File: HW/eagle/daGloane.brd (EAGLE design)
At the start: 100 x 80 mm, 90 parts, among them IC1 MCP1252-33X50, U1 STM32F10XTXU6, X2 SPARKFUN-CONNECTORS_USB-MICROB

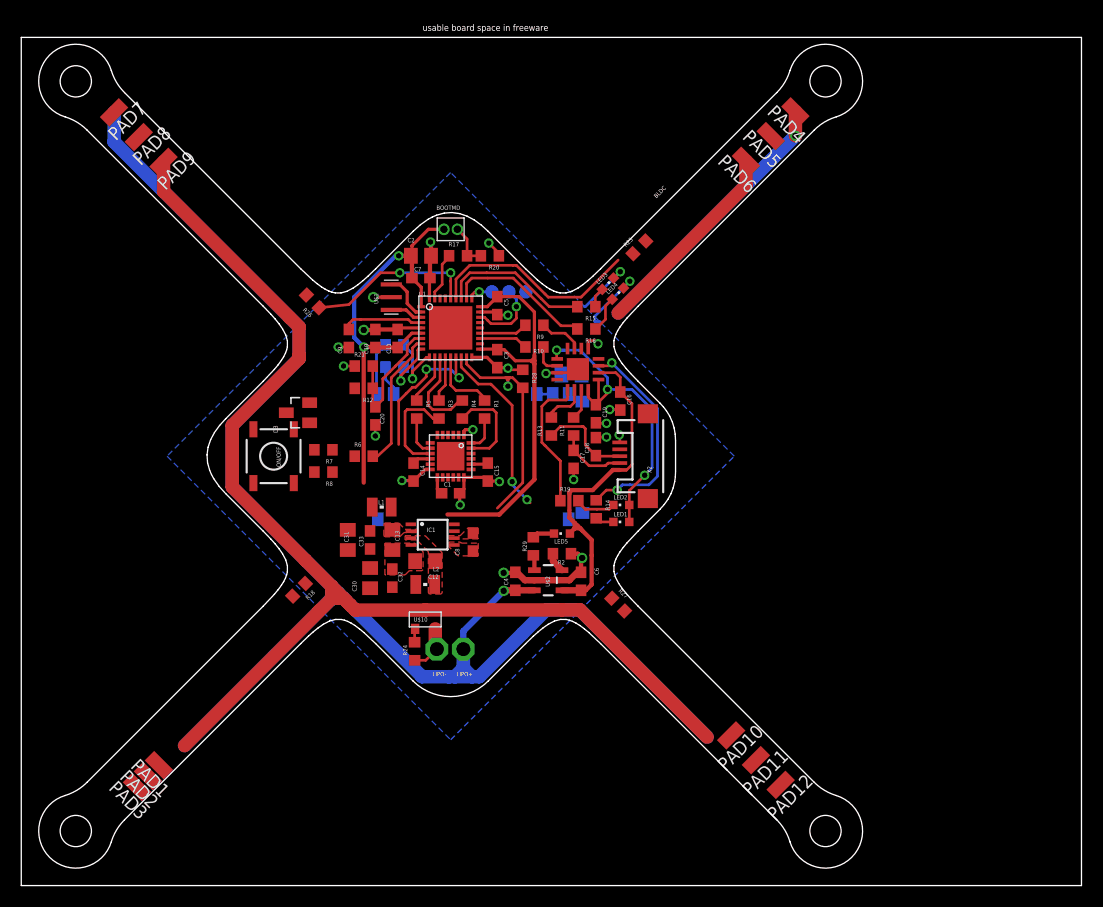
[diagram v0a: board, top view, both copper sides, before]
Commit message: DC/DC layout done
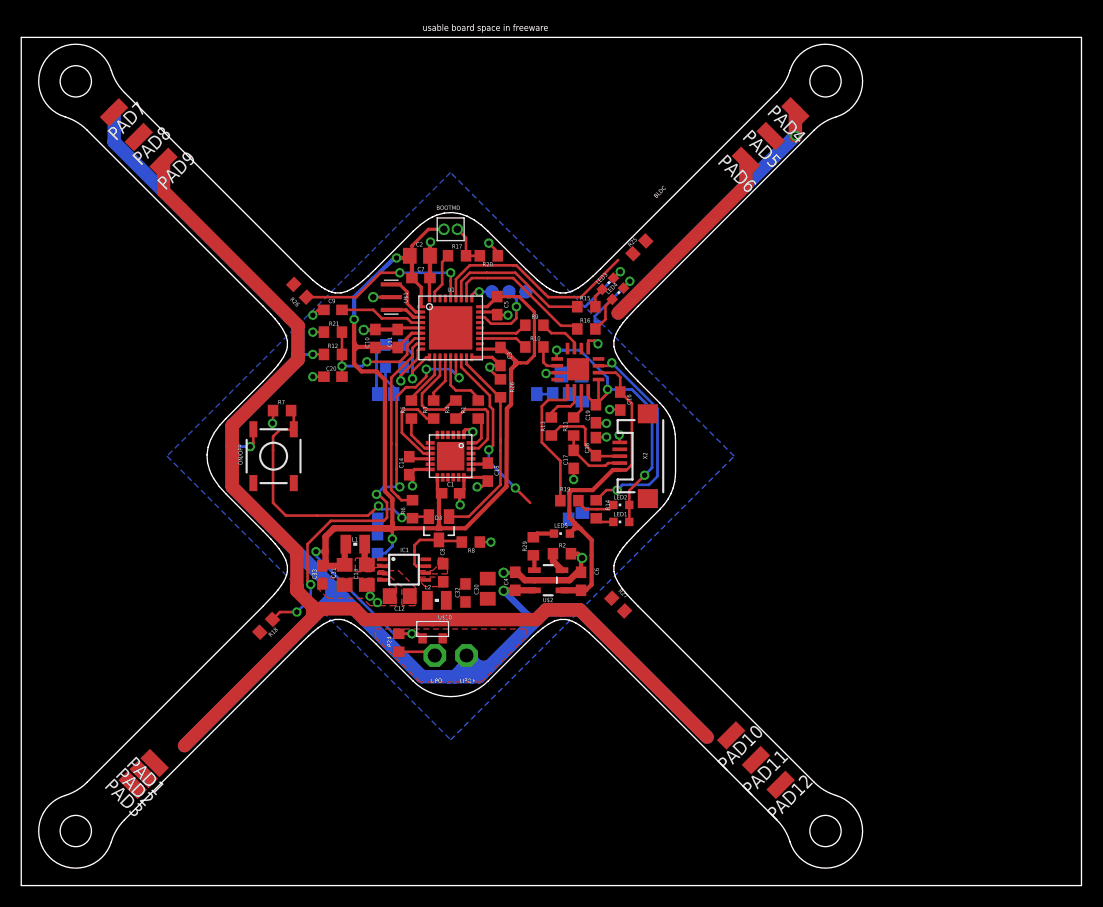
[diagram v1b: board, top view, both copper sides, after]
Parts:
- added R30: 1k, rcl:R0603
- moved D3 17.2 mm to (39.4, 33.7), turned to 180 degrees
- moved R8 15.4 mm to (42.4, 32.4)
- moved C30 11.1 mm to (44.0, 28.0)
- moved C32 7.04 mm to (41.9, 27.6)
- moved R6 6.79 mm to (36.9, 35.5), turned to 90 degrees
- moved C33 5.58 mm to (28.4, 29.3)
- moved C20 5.45 mm to (29.4, 48.0), turned to 180 degrees
- moved R7 5.38 mm to (24.6, 44.8), turned to 0 degrees
- moved R18 4.60 mm to (23.1, 24.5)
- moved R12 4.32 mm to (29.4, 50.1)
- moved R21 4.32 mm to (29.4, 52.2)
- moved L1 4.30 mm to (31.5, 32.2)
- moved IC1 4.26 mm to (36.1, 29.8)
- moved C12 4.08 mm to (35.7, 27.3)
- moved C13 4.08 mm to (32.6, 29.3)
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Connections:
- new net N$26: R30.1, U$5.P$34
- net VCC: now also R30.2; no longer U$5.P$34
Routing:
- net VCC: track 83.0 -> 133.1 mm, vias 2 -> 5
- net MOT1: track 13.8 -> 41.8 mm, vias 2 -> 6
- net N$23: track 0.00 -> 26.4 mm, vias 0 -> 2
- net LIPO: track 168.5 -> 176.6 mm, vias 2 -> 4
- net PWR_ON: track 0.00 -> 7.52 mm
- net PWR_OFF: track 13.0 -> 17.6 mm
- net GND: track 74.7 -> 76.8 mm, vias 24 -> 28
- net N$46: track 0.00 -> 2.04 mm
- net N$26: track 0.00 -> 1.51 mm
- net PWR_ON_µC: track 20.8 -> 19.5 mm, vias 1 -> 0
- net N$13: track 9.02 -> 7.96 mm
- net MOT4: track 16.1 -> 17.0 mm
- net VOLTAGE: track 12.6 -> 13.2 mm, vias 0 -> 2
- net N$18: track 9.52 -> 8.89 mm
- net SPI1_MOSI: track 6.57 -> 5.97 mm

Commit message: layout of center piece is done!
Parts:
- moved R14 15.1 mm to (52.0, 50.4), turned to 0 degrees
- moved LED1 12.7 mm to (54.9, 46.9), turned to 270 degrees
- moved C6 7.72 mm to (46.6, 33.3), turned to 0 degrees
- moved R2 7.00 mm to (44.0, 31.5), turned to 90 degrees
- moved C17 3.89 mm to (49.4, 37.4)
- moved R11 3.89 mm to (49.4, 40.5)
- moved R13 3.89 mm to (47.3, 40.5)
- moved U$2 3.58 mm to (46.5, 30.4), turned to 0 degrees
- moved C19 3.55 mm to (51.5, 42.2)
- moved C18 3.48 mm to (51.5, 39.2)
- moved R27 3.45 mm to (58.0, 23.5)
- moved U$4 3.32 mm to (50.1, 46.4)
- moved C16 2.66 mm to (54.0, 44.8)
- moved R29 2.60 mm to (49.3, 29.6)
- moved LED2 2.48 mm to (54.9, 34.1)
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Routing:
- net LIPO: track 176.6 -> 219.2 mm, vias 4 -> 6
- net MOT_GND: track 134.7 -> 157.8 mm
- net N$22: track 0.00 -> 20.4 mm
- net MOT2: track 16.7 -> 34.3 mm, vias 2 -> 6
- net N$11: track 20.6 -> 5.24 mm, vias 2 -> 0
- net VCC: track 133.1 -> 144.4 mm, vias 5 -> 6
- net N$43: track 1.42 -> 7.11 mm, vias 0 -> 2
- net D+: track 8.87 -> 12.2 mm
- net D-: track 6.52 -> 9.82 mm
- net N$14: track 1.76 -> 4.64 mm
- net N$21: track 2.88 -> 5.70 mm
- net N$1: track 3.98 -> 1.57 mm
- net N$12: track 13.2 -> 15.1 mm
- net GND: track 76.8 -> 78.3 mm, vias 28 -> 29
- net LED1: track 14.2 -> 12.9 mm
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- added copper zone on layer 1, net LIPO
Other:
- board text removed: "BLDC"

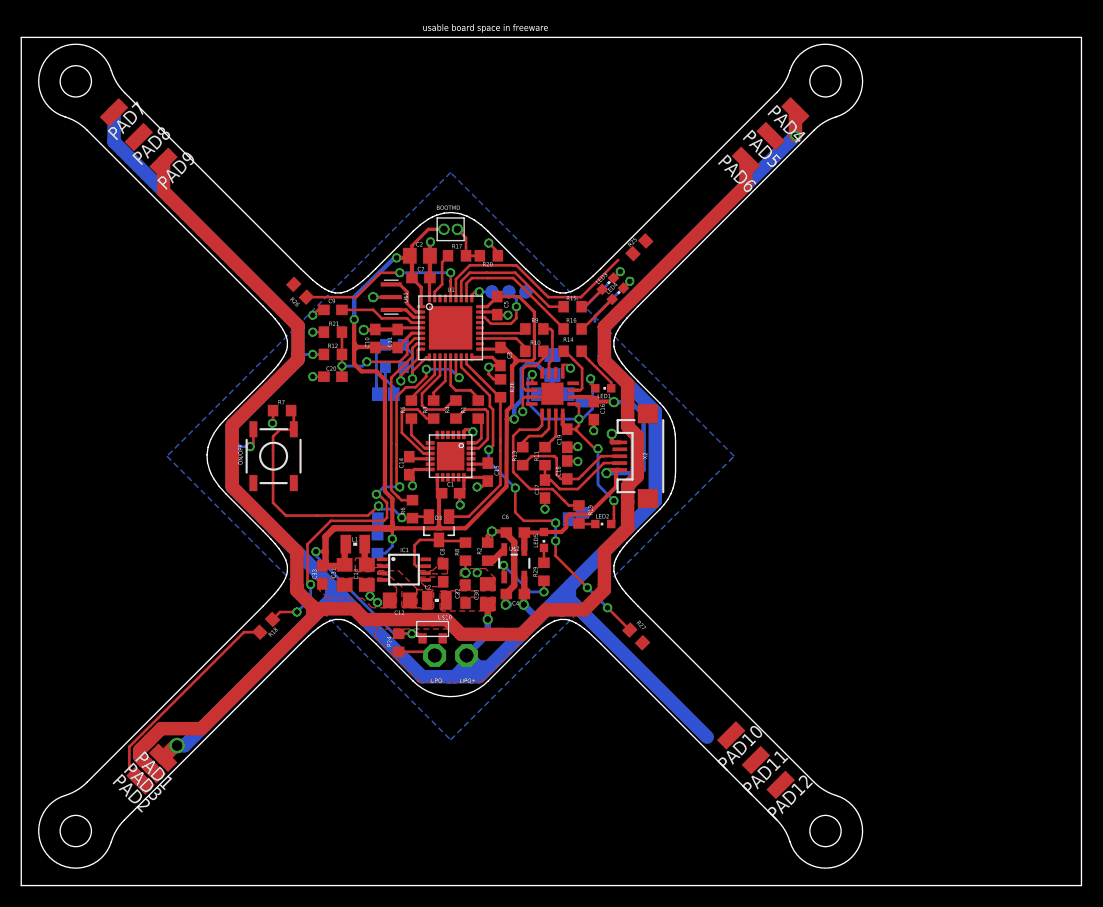
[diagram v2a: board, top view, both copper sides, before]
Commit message: testpads replaced with HK03 bldc controller symbol & package
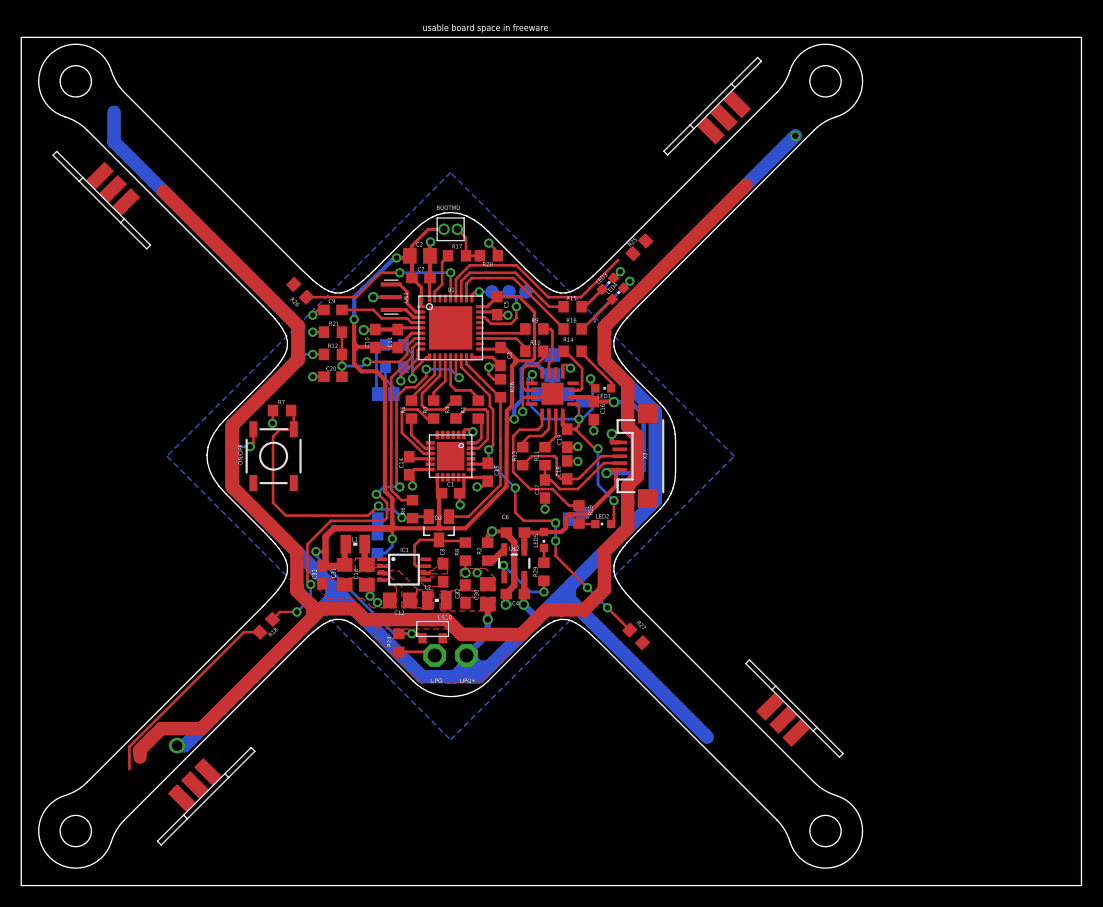
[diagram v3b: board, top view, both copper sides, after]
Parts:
- removed PAD1, PAD10, PAD11, PAD12, PAD2, PAD3, PAD4, PAD5, PAD6, PAD7, PAD8, PAD9: (no value), daGloane:SMD1,27-2,54
- added U$6, U$7, U$8, U$9: 3A_BLDC_CONTROLLER, daGloane:3A_BLDC_CONTROLLER
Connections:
- net LIPO: now also U$6.2, U$7.2, U$8.2, U$9.2; no longer PAD1.1, PAD10.1, PAD4.1, PAD7.1
- net MOT_GND: now also U$6.1, U$7.1, U$8.1, U$9.1; no longer PAD12.1, PAD3.1, PAD6.1, PAD9.1
- net N$22: now also U$6.3; no longer PAD2.1
- net N$39: now also U$7.3; no longer PAD11.1
- net N$40: now also U$8.3; no longer PAD5.1
- net N$41: now also U$9.3; no longer PAD8.1
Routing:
- net MOT_GND: track 157.8 -> 151.2 mm
- net LIPO: track 219.2 -> 215.2 mm
- net N$22: track 20.4 -> 18.9 mm
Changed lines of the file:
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@@
 <attribute name="VALUE" x="55.934540625" y="22.691778125" size="0.4064" layer="27" rot="R315"/>
 </element>
-<element name="PAD1" library="daGloane" package="SMD1,27-2,54" value="" x="13.38700625" y="12.055634375" rot="R45"/>
-<element name="PAD2" library="daGloane" package="SMD1,27-2,54" value="" x="11.25355625" y="9.92218125" rot="R45"/>
-<element name="PAD3" library="daGloane" package="SMD1,27-2,54" value="" x="12.320103125" y="10.988728125" rot="R45"/>
-<element name="PAD4" library="daGloane" package="SMD1,27-2,54" value="" x="73.018378125" y="73.028425" rot="R45"/>
-<element name="PAD5" library="daGloane" package="SMD1,27-2,54" value="" x="70.684925" y="70.694971875" rot="R45"/>
-<element name="PAD6" library="daGloane" package="SMD1,27-2,54" value="" x="68.351471875" y="68.361521875" rot="R45"/>
-<element name="PAD7" library="daGloane" package="SMD1,27-2,54" value="" x="8.752334375" y="72.93345" rot="R135"/>
-<element name="PAD8" library="daGloane" package="SMD1,27-2,54" value="" x="11.0857875" y="70.6" rot="R135"/>
-<element name="PAD9" library="daGloane" package="SMD1,27-2,54" value="" x="13.419240625" y="68.26655" rot="R135"/>
-<element name="PAD10" library="daGloane" package="SMD1,27-2,54" value="" x="66.95944375" y="14.164821875" rot="R135"/>
-<element name="PAD11" library="daGloane" package="SMD1,27-2,54" value="" x="69.29289375" y="11.83136875" rot="R135"/>
-<element name="PAD12" library="daGloane" package="SMD1,27-2,54" value="" x="71.626346875" y="9.497915625" rot="R135"/>
 <element name="R28" library="rcl" package="R0603" value="10k" x="45.2" y="46.9" smashed="yes" rot="R270">
 <attribute name="NAME" x="46.089" y="47.489" size="0.4064" layer="25" rot="R270"/>
@@
 <attribute name="VALUE" x="35.632" y="33.089" size="1.27" layer="28" rot="MR270"/>
 </element>
+<element name="U$6" library="daGloane" package="3A_BLDC_CONTROLLER" value="3A_BLDC_CONTROLLER" x="16.38189375" y="9.48379375" rot="R315"/>
+<element name="U$7" library="daGloane" package="3A_BLDC_CONTROLLER" value="3A_BLDC_CONTROLLER" x="71.870178125" y="15.635859375" rot="R45"/>
+<element name="U$8" library="daGloane" package="3A_BLDC_CONTROLLER" value="3A_BLDC_CONTROLLER" x="66.270834375" y="72.446328125" rot="R135"/>
+<element name="U$9" library="daGloane" package="3A_BLDC_CONTROLLER" value="3A_BLDC_CONTROLLER" x="8.655340625" y="65.70975625" rot="R225"/>
 </elements>
 <signals>
@@
 <contactref element="C32" pad="2"/>
 <wire x1="47.45" y1="27.5" x2="47.45" y2="29.0999" width="0.6096" layer="1"/>
-<contactref element="PAD1" pad="1"/>
-<contactref element="PAD10" pad="1"/>
-<contactref element="PAD4" pad="1"/>
-<contactref element="PAD7" pad="1"/>
 <wire x1="8.752334375" y1="72.93345" x2="8.752334375" y2="70.147665625" width="1.27" layer="16"/>
 <wire x1="8.752334375" y1="70.147665625" x2="15.1" y2="63.8" width="1.27" layer="16"/>
@@
 <wire x1="41.7" y1="20.5" x2="41.6" y2="20.4" width="1.27" layer="16"/>
 <wire x1="41.6" y1="20.4" x2="40.9" y2="19.7" width="1.27" layer="16"/>
-<wire x1="73.018378125" y1="73.028425" x2="73.018378125" y2="70.718378125" width="1.27" layer="1"/>
 <wire x1="73.018378125" y1="70.718378125" x2="56.3" y2="54" width="1.27" layer="16"/>
 <via x="73.018378125" y="70.718378125" extent="1-16" drill="0.6"/>
@@
 <via x="14.7" y="13.2" extent="1-16" drill="1"/>
 <wire x1="14.7" y1="13.2" x2="14.531371875" y2="13.2" width="1.27" layer="1"/>
-<wire x1="14.531371875" y1="13.2" x2="13.38700625" y2="12.055634375" width="1.27" layer="1"/>
-<wire x1="64.7" y1="14" x2="66.95944375" y2="14.164821875" width="0" layer="19" extent="1-16"/>
-<wire x1="8.752334375" y1="72.93345" x2="8.752334375" y2="72.93345" width="0" layer="19" extent="1-16"/>
+<contactref element="U$6" pad="2"/>
+<contactref element="U$7" pad="2"/>
+<contactref element="U$8" pad="2"/>
+<contactref element="U$9" pad="2"/>
+<wire x1="66.270834375" y1="72.446328125" x2="8.655340625" y2="65.70975625" width="0" layer="19" extent="1-1"/>
+<wire x1="71.870178125" y1="15.635859375" x2="66.270834375" y2="72.446328125" width="0" layer="19" extent="1-1"/>
+<wire x1="16.38189375" y1="9.48379375" x2="71.870178125" y2="15.635859375" width="0" layer="19" extent="1-1"/>
+<wire x1="14.531371875" y1="13.2" x2="16.38189375" y2="9.48379375" width="0" layer="19" extent="1-1"/>
 </signal>
 <signal name="VOLTAGE">
@@
 <wire x1="51.4" y1="34.7" x2="51.6" y2="34.9" width="0.4" layer="1"/>
 <wire x1="51.6" y1="34.9" x2="51.7" y2="35" width="0.4" layer="1"/>
-<wire x1="51.7" y1="35" x2="53.5" y2="35" width="0.4" layer="1"/>
-<wire x1="53.5" y1="35" x2="53.9" y2="35.4" width="0.4" layer="1"/>
-<wire x1="56.1" y1="37.7" x2="56.1" y2="37.6" width="0.4" layer="1"/>
-<wire x1="56.1" y1="37.6" x2="53.9" y2="35.4" width="0.4" layer="1"/>
+<wire x1="51.7" y1="35" x2="53.4" y2="35" width="0.4" layer="1"/>
+<wire x1="53.4" y1="35" x2="53.8" y2="35.4" width="0.4" layer="1"/>
+<wire x1="56.1" y1="37.7" x2="53.8" y2="35.4" width="0.4" layer="1"/>
 <wire x1="49.3" y1="33.35" x2="49.25" y2="33.3" width="0.4" layer="1"/>
 <wire x1="49.25" y1="33.3" x2="47.45" y2="33.3" width="0.4" layer="1"/>
@@
 <signal name="MOT_GND">
 <contactref element="U$10" pad="3"/>
-<contactref element="PAD3" pad="1"/>
-<contactref element="PAD12" pad="1"/>
-<contactref element="PAD6" pad="1"/>
-<contactref element="PAD9" pad="1"/>
-<wire x1="13.419240625" y1="68.26655" x2="13.419240625" y2="65.480759375" width="1.27" layer="1"/>
 <wire x1="13.419240625" y1="65.480759375" x2="25.3" y2="53.6" width="1.27" layer="1"/>
 <wire x1="25.3" y1="53.6" x2="26.1" y2="52.8" width="1.27" layer="1"/>
@@
 <wire x1="27.7" y1="25.5" x2="27.5" y2="25.3" width="1.27" layer="1"/>
 <wire x1="27.5" y1="25.3" x2="17.25" y2="15.05" width="1.27" layer="1"/>
-<wire x1="68.351471875" y1="68.361521875" x2="68.351471875" y2="66.051471875" width="1.27" layer="1"/>
 <wire x1="68.351471875" y1="66.051471875" x2="56.3" y2="54" width="1.27" layer="1"/>
 <wire x1="38.8" y1="25.085" x2="40.115" y2="25.085" width="1.27" layer="1"/>
@@
 <wire x1="53.1" y1="26" x2="55" y2="27.9" width="1.27" layer="1"/>
 <wire x1="55" y1="27.9" x2="55" y2="28.4" width="1.27" layer="1"/>
-<wire x1="12.320103125" y1="10.988728125" x2="11.2" y2="12.10883125" width="1.27" layer="1"/>
 <wire x1="11.2" y1="12.10883125" x2="11.2" y2="12.5" width="1.27" layer="1"/>
 <wire x1="11.2" y1="12.5" x2="11.2" y2="12.8" width="1.27" layer="1"/>
@@
 <wire x1="15.9" y1="14.8" x2="17" y2="14.8" width="1.27" layer="1"/>
 <wire x1="17" y1="14.8" x2="17.25" y2="15.05" width="1.27" layer="1"/>
-<wire x1="55" y1="27.9" x2="71.626346875" y2="9.497915625" width="0" layer="19" extent="1-1"/>
+<contactref element="U$6" pad="1"/>
+<contactref element="U$7" pad="1"/>
+<contactref element="U$8" pad="1"/>
+<contactref element="U$9" pad="1"/>
+<wire x1="17.619328125" y1="10.721228125" x2="11.2" y2="12.10883125" width="0" layer="19" extent="1-1"/>
+<wire x1="70.632740625" y1="16.87329375" x2="17.619328125" y2="10.721228125" width="0" layer="19" extent="1-1"/>
+<wire x1="65.033396875" y1="71.208890625" x2="70.632740625" y2="16.87329375" width="0" layer="19" extent="1-1"/>
+<wire x1="9.892775" y1="64.47231875" x2="65.033396875" y2="71.208890625" width="0" layer="19" extent="1-1"/>
 </signal>
 <signal name="N$43">
@@
 <signal name="N$22">
 <contactref element="R18" pad="2"/>
-<contactref element="PAD2" pad="1"/>
-<wire x1="11.25355625" y1="9.92218125" x2="10.2" y2="10.9757375" width="0.254" layer="1"/>
 <wire x1="10.2" y1="10.9757375" x2="10.2" y2="13.1" width="0.254" layer="1"/>
 <wire x1="10.2" y1="13.1" x2="20.99895625" y2="23.89895625" width="0.254" layer="1"/>
 <wire x1="20.99895625" y1="23.89895625" x2="22.49895625" y2="23.89895625" width="0.254" layer="1"/>
+<contactref element="U$6" pad="3"/>
+<wire x1="15.14445625" y1="8.24635625" x2="10.2" y2="10.9757375" width="0" layer="19" extent="1-1"/>
 </signal>
 <signal name="N$39">
 <contactref element="R27" pad="2"/>
-<contactref element="PAD11" pad="1"/>
-<wire x1="69.29289375" y1="11.83136875" x2="58.601040625" y2="22.89895625" width="0" layer="19" extent="1-1"/>
+<contactref element="U$7" pad="3"/>
+<wire x1="73.1076125" y1="14.398421875" x2="58.601040625" y2="22.89895625" width="0" layer="19" extent="1-1"/>
 </signal>
 <signal name="N$40">
 <contactref element="R25" pad="2"/>
-<contactref element="PAD5" pad="1"/>
-<wire x1="58.901040625" y1="60.801040625" x2="70.684925" y2="70.694971875" width="0" layer="19" extent="1-1"/>
+<contactref element="U$8" pad="3"/>
+<wire x1="67.50826875" y1="73.6837625" x2="58.901040625" y2="60.801040625" width="0" layer="19" extent="1-1"/>
 </signal>
 <signal name="N$41">
 <contactref element="R26" pad="2"/>
-<contactref element="PAD8" pad="1"/>
-<wire x1="11.0857875" y1="70.6" x2="25.69895625" y2="56.701040625" width="0" layer="19" extent="1-1"/>
+<contactref element="U$9" pad="3"/>
+<wire x1="7.417903125" y1="66.947190625" x2="25.69895625" y2="56.701040625" width="0" layer="19" extent="1-1"/>
 </signal>
 <signal name="N$26">

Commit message: routing completed!! optimization pending
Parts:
- moved U$6 4.92 mm to (12.5, 12.5)
- moved U$9 4.75 mm to (12.5, 68.5)
- moved U$7 4.60 mm to (68.5, 12.5)
- moved U$8 4.53 mm to (68.5, 68.5)
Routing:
- net N$41: track 0.00 -> 22.5 mm
- net N$39: track 0.00 -> 20.5 mm, vias 0 -> 2
- net MOT_GND: track 151.2 -> 170.9 mm
- net N$40: track 0.00 -> 17.8 mm, vias 0 -> 2
- net LIPO: track 215.2 -> 219.4 mm, vias 6 -> 8
- net MOT3: track 20.4 -> 22.0 mm
- net GND: track 78.3 -> 79.7 mm
- net N$22: track 18.9 -> 19.7 mm
